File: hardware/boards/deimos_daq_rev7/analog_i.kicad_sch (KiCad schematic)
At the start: 1 part

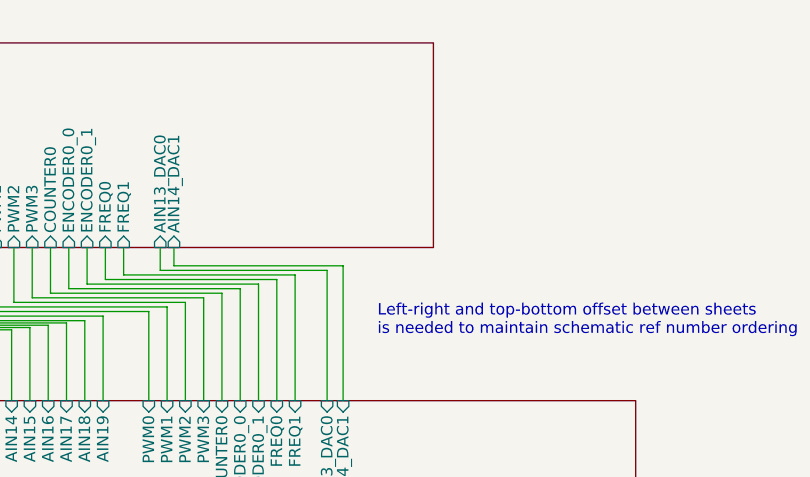
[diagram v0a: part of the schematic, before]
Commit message: wip to export more gpio pins
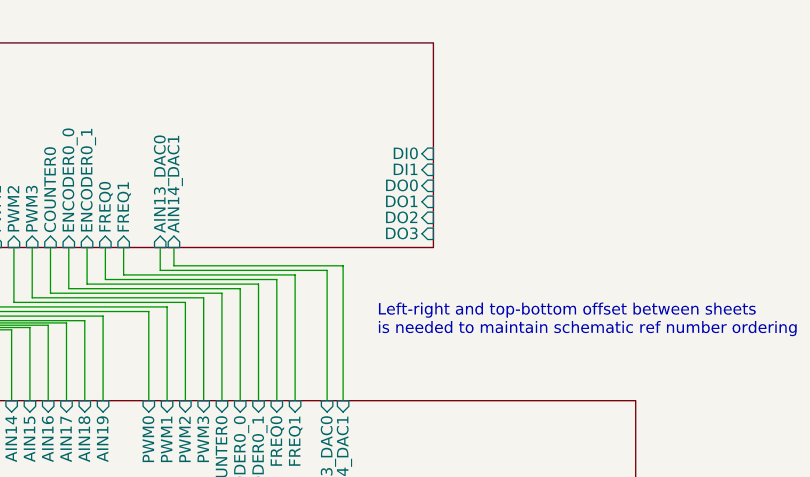
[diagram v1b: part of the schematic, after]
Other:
- sheet base ports: added DI0, DI1, DO0, DO1, DO2, DO3; removed none
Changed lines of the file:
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@@
+			)
+		)
+		(pin "DI0" input
+			(at 109.601 28.956 0)
+			(effects
+				(font
+					(size 1.27 1.27)
+				)
+				(justify right)
+			)
+		)
+		(pin "DI1" input
+			(at 109.601 30.734 0)
+			(effects
+				(font
+					(size 1.27 1.27)
+				)
+				(justify right)
+			)
+		)
+		(pin "DO1" input
+			(at 109.601 34.29 0)
+			(effects
+				(font
+					(size 1.27 1.27)
+				)
+				(justify right)
+			)
+		)
+		(pin "DO2" input
+			(at 109.601 36.068 0)
+			(effects
+				(font
+					(size 1.27 1.27)
+				)
+				(justify right)
+			)
+		)
+		(pin "DO3" input
+			(at 109.601 37.846 0)
+			(effects
+				(font
+					(size 1.27 1.27)
+				)
+				(justify right)
+			)
+		)
+		(pin "DO0" input
+			(at 109.601 32.512 0)
+			(effects
+				(font
+					(size 1.27 1.27)
+				)
+				(justify right)
 			)
 		)

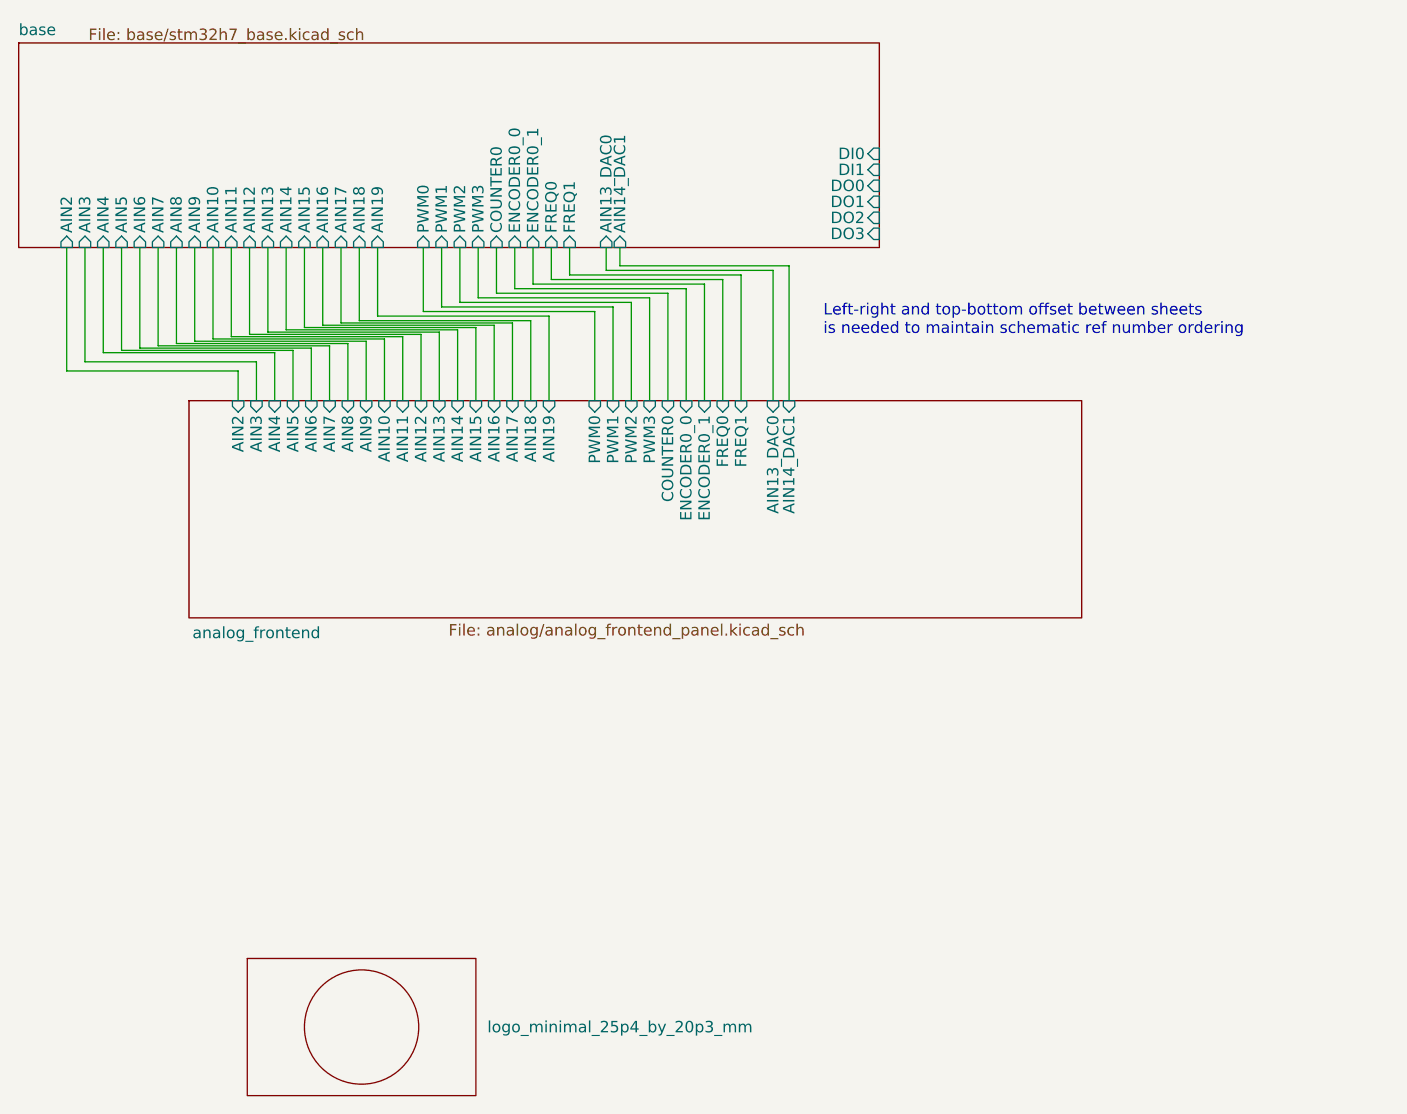
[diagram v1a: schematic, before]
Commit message: route gpio
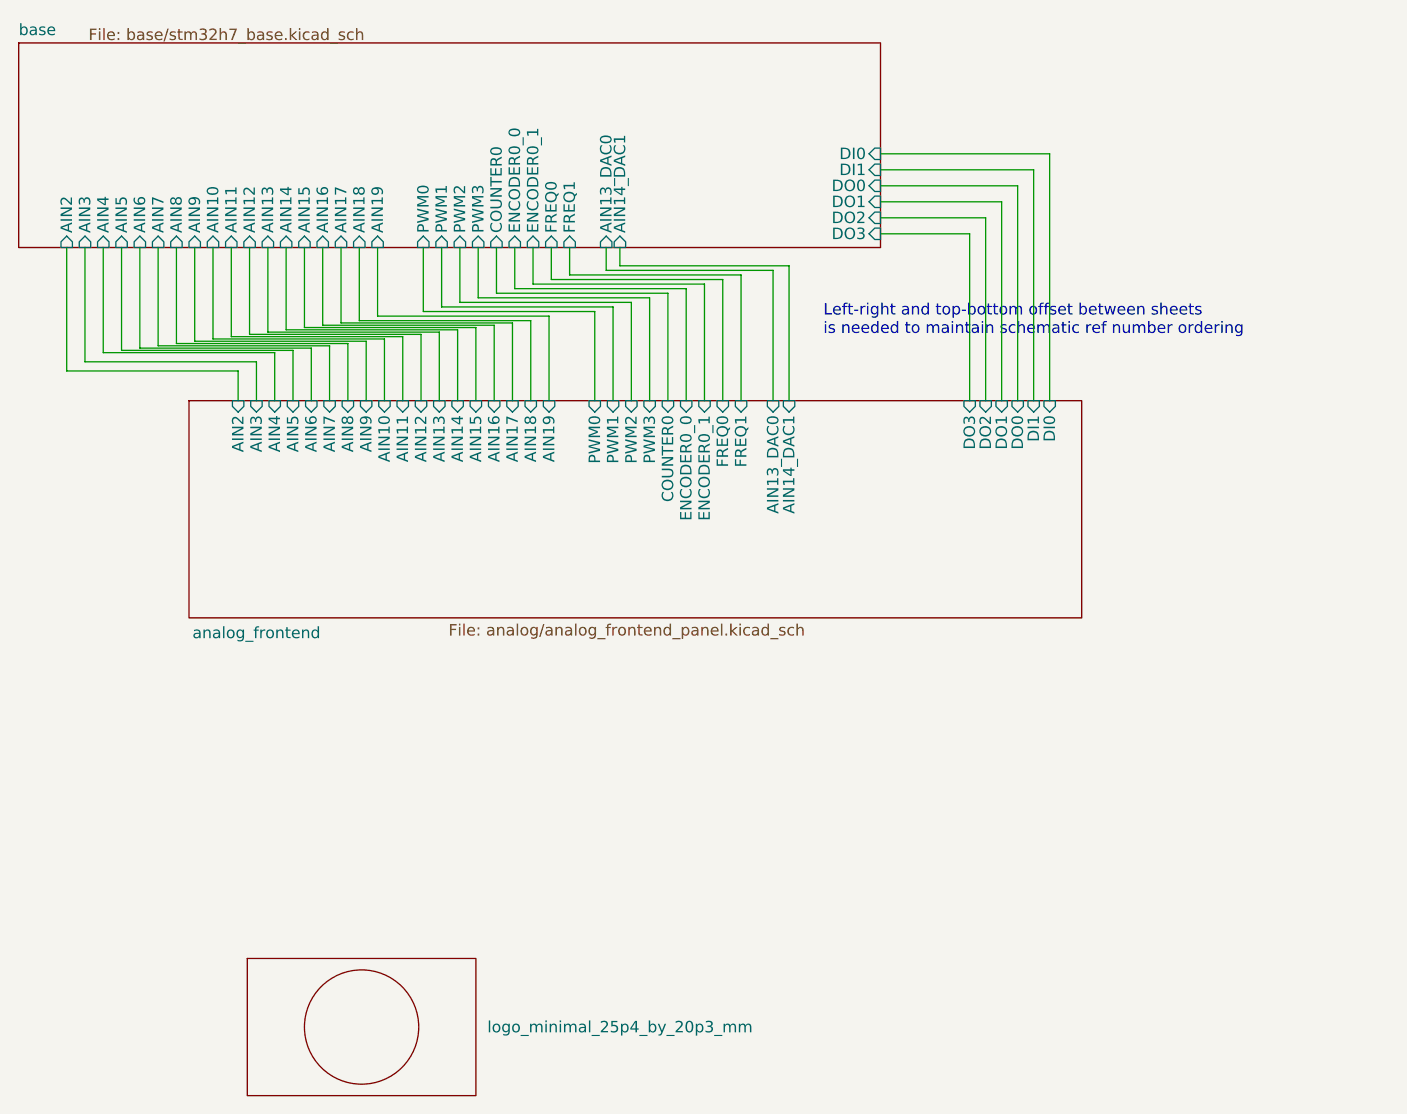
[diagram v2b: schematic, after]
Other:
- sheet analog_frontend ports: added DI0, DI1, DO0, DO1, DO2, DO3; removed none
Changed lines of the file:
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@@
+	(wire
+		(pts
+			(xy 121.412 56.388) (xy 121.412 36.068)
+		)
+		(stroke
+			(width 0)
+			(type default)
+		)
+	)
+	(wire
+		(pts
+			(xy 121.412 36.068) (xy 109.728 36.068)
+		)
+		(stroke
+			(width 0)
+			(type default)
+		)
+	)
 	(wire
 		(pts
@@
 	(wire
 		(pts
+			(xy 119.634 37.846) (xy 119.634 56.388)
+		)
+		(stroke
+			(width 0)
+			(type default)
+		)
+	)
+	(wire
+		(pts
 			(xy 70.866 47.498) (xy 70.866 56.388)
 		)
@@
 	(wire
 		(pts
+			(xy 128.524 28.956) (xy 128.524 56.388)
+		)
+		(stroke
+			(width 0)
+			(type default)
+		)
+	)
+	(wire
+		(pts
 			(xy 79.248 39.37) (xy 79.248 41.91)
 		)
@@
 	(wire
 		(pts
+			(xy 109.728 28.956) (xy 128.524 28.956)
+		)
+		(stroke
+			(width 0)
+			(type default)
+		)
+	)
+	(wire
+		(pts
 			(xy 35.56 39.37) (xy 35.56 49.53)
 		)
@@
 	(wire
 		(pts
+			(xy 109.728 37.846) (xy 119.634 37.846)
+		)
+		(stroke
+			(width 0)
+			(type default)
+		)
+	)
+	(wire
+		(pts
 			(xy 27.432 50.546) (xy 46.482 50.546)
 		)
@@
 	(wire
 		(pts
+			(xy 109.728 32.512) (xy 124.968 32.512)
+		)
+		(stroke
+			(width 0)
+			(type default)
+		)
+	)
+	(wire
+		(pts
 			(xy 62.992 45.466) (xy 82.042 45.466)
 		)
@@
 	(wire
 		(pts
+			(xy 109.728 30.734) (xy 126.746 30.734)
+		)
+		(stroke
+			(width 0)
+			(type default)
+		)
+	)
+	(wire
+		(pts
+			(xy 126.746 30.734) (xy 126.746 56.388)
+		)
+		(stroke
+			(width 0)
+			(type default)
+		)
+	)
+	(wire
+		(pts
 			(xy 43.688 39.37) (xy 43.688 48.514)
 		)
@@
 	(wire
 		(pts
+			(xy 109.728 34.29) (xy 123.19 34.29)
+		)
+		(stroke
+			(width 0)
+			(type default)
+		)
+	)
+	(wire
+		(pts
 			(xy 52.578 49.784) (xy 52.578 56.388)
 		)
@@
 	(wire
 		(pts
+			(xy 123.19 34.29) (xy 123.19 56.388)
+		)
+		(stroke
+			(width 0)
+			(type default)
+		)
+	)
+	(wire
+		(pts
 			(xy 51.816 39.37) (xy 51.816 47.498)
 		)
@@
 		(pts
 			(xy 23.368 51.054) (xy 42.418 51.054)
+		)
+		(stroke
+			(width 0)
+			(type default)
+		)
+	)
+	(wire
+		(pts
+			(xy 124.968 32.512) (xy 124.968 56.388)
 		)
 		(stroke
@@
 	(sheet
 		(at 13.97 16.637)
-		(size 95.631 22.733)
+		(size 95.758 22.733)
 		(stroke
 			(width 0.1524)
@@
 		)
 		(pin "DI0" input
-			(at 109.601 28.956 0)
+			(at 109.728 28.956 0)
 			(effects
 				(font
@@
 		)
 		(pin "DI1" input
-			(at 109.601 30.734 0)
+			(at 109.728 30.734 0)
 			(effects
 				(font
@@
 		)
 		(pin "DO1" input
-			(at 109.601 34.29 0)
+			(at 109.728 34.29 0)
 			(effects
 				(font
@@
 		)
 		(pin "DO2" input
-			(at 109.601 36.068 0)
+			(at 109.728 36.068 0)
 			(effects
 				(font
@@
 		)
 		(pin "DO3" input
-			(at 109.601 37.846 0)
+			(at 109.728 37.846 0)
 			(effects
 				(font
@@
 		)
 		(pin "DO0" input
-			(at 109.601 32.512 0)
+			(at 109.728 32.512 0)
 			(effects
 				(font
@@
 			(effects
 				(font
+					(size 1.27 1.27)
+				)
+				(justify right)
+			)
+		)
+		(pin "DO0" input
+			(at 124.968 56.388 90)
+			(effects
+				(font
+					(size 1.27 1.27)
+				)
+				(justify right)
+			)
+		)
+		(pin "DI1" input
+			(at 126.746 56.388 90)
+			(effects
+				(font
+					(size 1.27 1.27)
+				)
+				(justify right)
+			)
+		)
+		(pin "DO3" input
+			(at 119.634 56.388 90)
+			(effects
+				(font
+					(size 1.27 1.27)
+				)
+				(justify right)
+			)
+		)
+		(pin "DO1" input
+			(at 123.19 56.388 90)
+			(effects
+				(font
+					(size 1.27 1.27)
+				)
+				(justify right)
+			)
+		)
+		(pin "DO2" input
+			(at 121.412 56.388 90)
+			(effects
+				(font
+					(size 1.27 1.27)
+				)
+				(justify right)
+			)
+		)
+		(pin "DI0" input
+			(at 128.524 56.388 90)
+			(effects
+				(font
